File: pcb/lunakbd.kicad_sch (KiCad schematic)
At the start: 56 parts, among them SW1 Switch, SW10 Switch, SW11 Switch, SW12 Switch, SW13 Switch, SW14 Switch, SW15 Switch, SW16 Switch, SW17 Switch, SW18 Switch, SW19 Switch, SW2 Switch, SW20 Switch, SW21 Switch, SW22 Switch, SW23 Switch, SW24 Switch, SW25 Switch, SW26 Switch, SW27 Switch, SW28 Switch, SW3 Switch, SW4 Switch, SW5 Switch, SW6 Switch, SW7 Switch, SW8 Switch, SW9 Switch

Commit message: feat: pcb layout adjustments
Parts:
- SW28: footprint PCM_Switch_Keyboard_Cherry_MX:SW_Cherry_MX_PCB_1.00u -> PCM_Switch_Keyboard_Cherry_MX:SW_Cherry_MX_PCB_1.25u_90deg
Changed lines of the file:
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@@
 			)
 		)
-		(property "Footprint" "PCM_Switch_Keyboard_Cherry_MX:SW_Cherry_MX_PCB_1.00u"
+		(property "Footprint" "PCM_Switch_Keyboard_Cherry_MX:SW_Cherry_MX_PCB_1.25u_90deg"
 			(at 266.7 134.62 0)
 			(effects

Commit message: feat: complete schematic design
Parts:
- added D29: Diode, Diode_SMD:D_SOD-123, symbol Device:D_Small
- added J1: TRRS-PJ-320A, Connector_Audio:Jack_3.5mm_PJ320E_Horizontal, symbol Connector_Audio:AudioJack4
- added J2: Battery_Socket, Connector_JST:JST_PH_S2B-PH-K_1x02_P2.00mm_Horizontal, symbol Connector:Conn_01x02_Socket
- added J3: Conn_Display, kbd:OLED, symbol Connector_Generic:Conn_01x04
- added SW29: Reset_Button, Keebio-Parts:SW_Tactile_SPST_Angled_MJTP1117-no-mount, symbol Switch:SW_Push
- added SW30: Battery_Switch, PCM_marbastlib-various:SW_MSK12C02-HB, symbol Switch:SW_SPDT
- added SW31: RotaryEncoder_SW, Rotary_Encoder:RotaryEncoder_Alps_EC11E-Switch_Vertical_H20mm, symbol Device:RotaryEncoder_Switch
- added U1: ProMicro, PCM_marbastlib-xp-promicroish:SuperMini_nRF52840_H_USBup, symbol PCM_marbastlib-promicroish:Arduino_ProMicro
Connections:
- net col-0: now also U1.19 (F6)
- net col-1: now also SW31.S1, U1.20 (F7)
- net col-2: now also U1.21 (B1)
- net col-3: now also U1.22 (B3)
- net col-4: now also U1.23 (B2)
- net col-5: now also U1.24 (B6)
- net row-0: now also U1.7 (D4)
- net row-1: now also U1.8 (C6)
- net row-2: now also U1.9 (D7)
- net row-3: now also U1.10 (E6)
- net row-4: now also D29.1 (K), U1.11 (B4)
- new net: D29.2 (A), SW31.S2
- new net B+: J2.2 (Pin_2), U1.13 (B0)
- new net B-: J2.1 (Pin_1), SW30.1 (A)
- new net GND: J1.R1, J3.4 (Pin_4), SW29.2, SW30.2 (B), SW31.C, U1.14 (GND), U1.3 (GND), U1.4 (GND)
- new net VCC: J1.R2, J3.3 (Pin_3), U1.16 (VCC)
- new net data: J1.T, U1.2 (D2-RX)
- new net enc-a: SW31.A, U1.17 (F4)
- new net enc-b: SW31.B, U1.18 (F5)
- new net reset: SW29.1, U1.15 (RST)
- new net sda: J3.1 (Pin_1), U1.5 (D1)
- new net sdl: J3.2 (Pin_2), U1.6 (D0)
- no-connect marks 0 -> 3

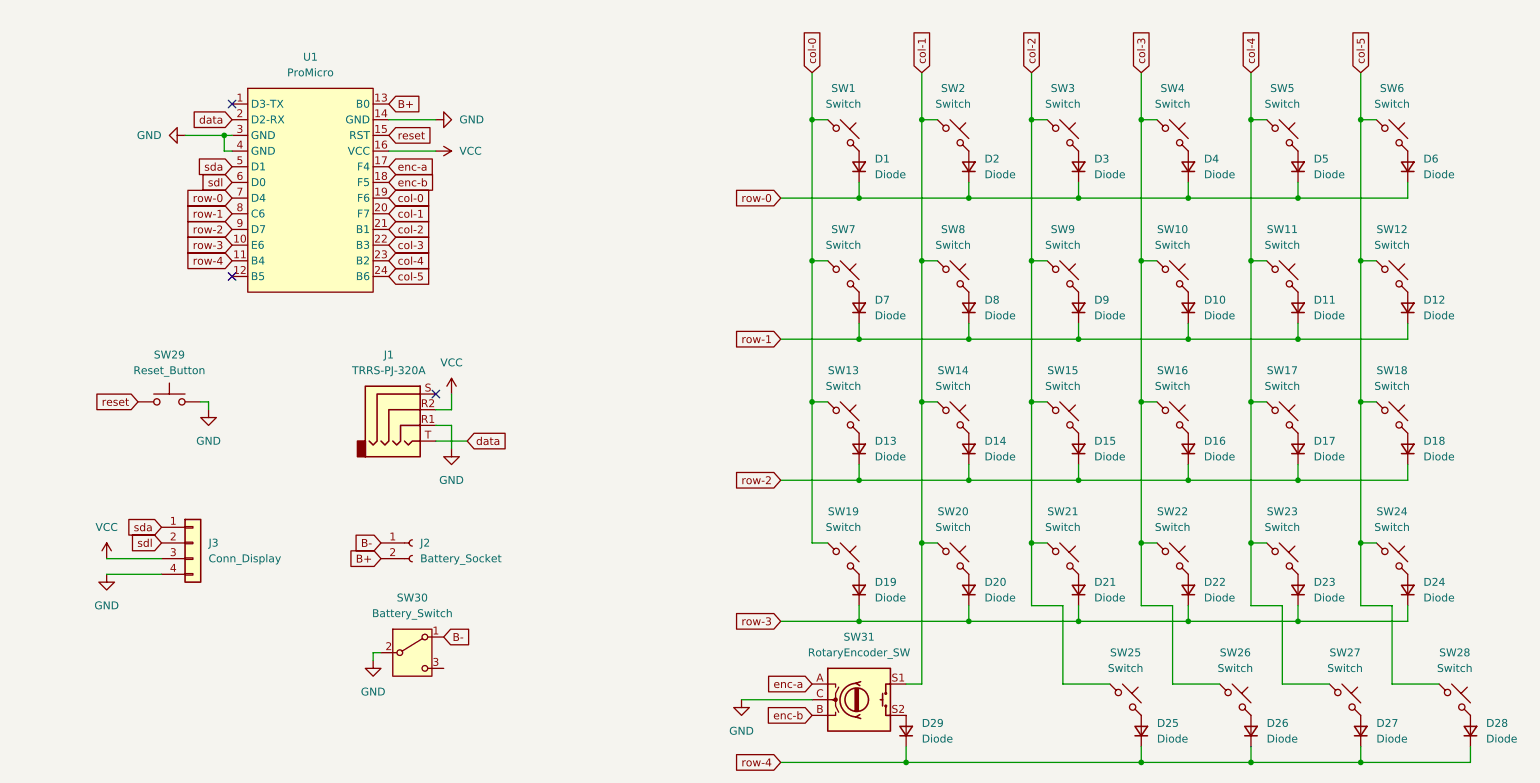
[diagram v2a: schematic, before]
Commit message: feat: update footprints and place promicro and oled display
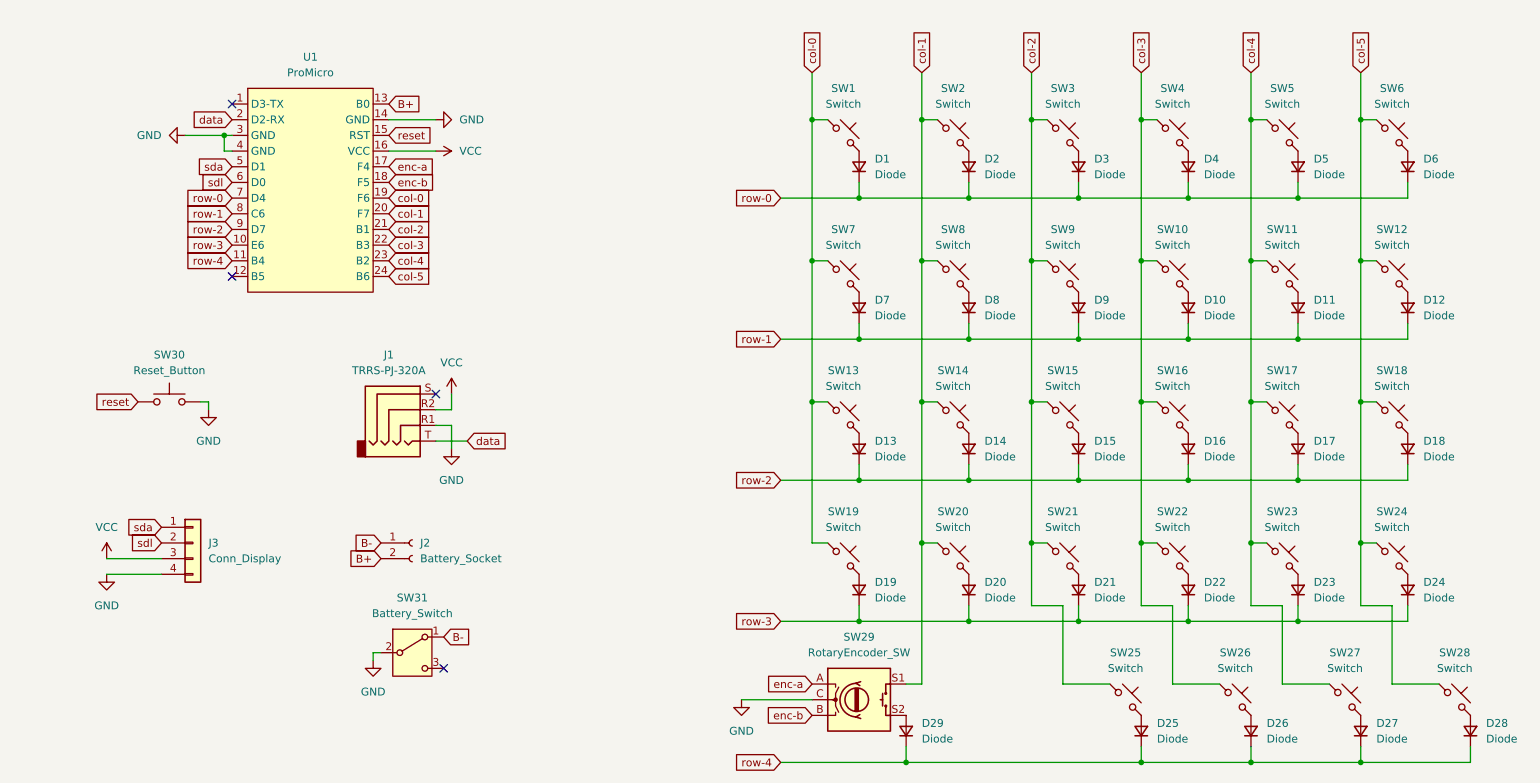
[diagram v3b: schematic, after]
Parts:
- J1: footprint Connector_Audio:Jack_3.5mm_PJ320E_Horizontal -> Keebio-Parts:TRRS-PJ-320A-no-Fmask
- SW1, SW10, SW11, SW12, SW13, SW14, SW15, SW16, SW17, SW18, SW19, SW2, SW20, SW21, SW22, SW23, SW24, SW25, SW26, SW27, SW3, SW4, SW5, SW6, SW7, SW8, SW9: footprint PCM_Switch_Keyboard_Cherry_MX:SW_Cherry_MX_PCB_1.00u -> PCM_Switch_Keyboard_Hotswap_Kailh:SW_Hotswap_Kailh_MX_1.00u
- SW28: footprint PCM_Switch_Keyboard_Cherry_MX:SW_Cherry_MX_PCB_1.25u_90deg -> PCM_Switch_Keyboard_Hotswap_Kailh:SW_Hotswap_Kailh_MX_1.25u_90deg
- SW30: renamed from SW29; footprint Keebio-Parts:SW_Tactile_SPST_Angled_MJTP1117-no-mount -> kbd:ResetSW
- SW31: renamed from SW30; footprint PCM_marbastlib-various:SW_MSK12C02-HB -> Button_Switch_SMD:SW_SPDT_PCM12
- renumbered SW31 to SW29
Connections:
- no-connect marks 3 -> 4

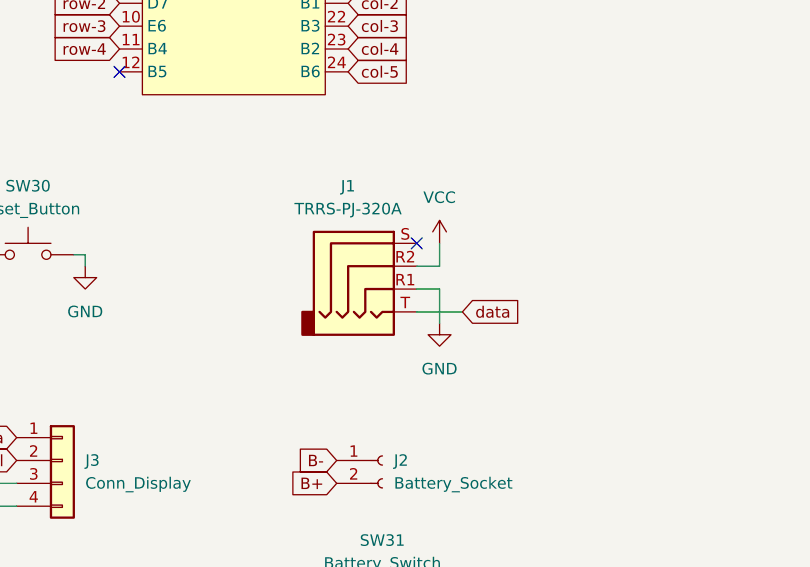
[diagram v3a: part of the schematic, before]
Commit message: feat: place trrs, battery socket and reset button
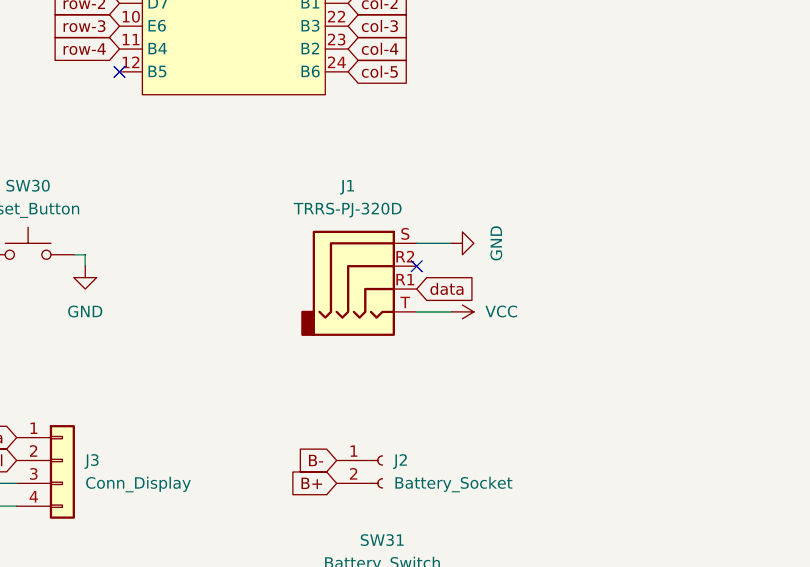
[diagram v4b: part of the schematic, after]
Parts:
- J1: value TRRS-PJ-320A -> TRRS-PJ-320D; footprint Keebio-Parts:TRRS-PJ-320A-no-Fmask -> Keebio-Parts:TRRS-PJ-320D
- SW30: footprint kbd:ResetSW -> kbd:SW_TL3330AF130QG
- SW31: footprint Button_Switch_SMD:SW_SPDT_PCM12 -> PCM_marbastlib-various:SW_MSK12C02-HB
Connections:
- net GND: now also J1.S; no longer J1.R1
- net VCC: now also J1.T; no longer J1.R2
- net data: now also J1.R1; no longer J1.T
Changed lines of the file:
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@@
 	)
 	(no_connect
-		(at 101.6 85.09)
-	)
-	(no_connect
 		(at 68.58 38.1)
 	)
@@
 		(at 102.87 129.54)
 	)
+	(no_connect
+		(at 101.6 87.63)
+	)
 	(wire
 		(pts
@@
 	(wire
 		(pts
-			(xy 182.88 109.22) (xy 180.34 109.22)
+			(xy 101.6 85.09) (xy 105.41 85.09)
 		)
 		(stroke
@@
 	(wire
 		(pts
-			(xy 223.52 99.06) (xy 241.3 99.06)
+			(xy 182.88 109.22) (xy 180.34 109.22)
 		)
 		(stroke
@@
 	(wire
 		(pts
-			(xy 170.18 76.2) (xy 187.96 76.2)
+			(xy 223.52 99.06) (xy 241.3 99.06)
 		)
 		(stroke
@@
 	(wire
 		(pts
-			(xy 182.88 63.5) (xy 180.34 63.5)
+			(xy 170.18 76.2) (xy 187.96 76.2)
 		)
 		(stroke
@@
 	(wire
 		(pts
-			(xy 170.18 73.66) (xy 170.18 76.2)
+			(xy 182.88 63.5) (xy 180.34 63.5)
 		)
 		(stroke
@@
 	(wire
 		(pts
-			(xy 203.2 119.38) (xy 198.12 119.38)
+			(xy 170.18 73.66) (xy 170.18 76.2)
 		)
 		(stroke
@@
 	(wire
 		(pts
-			(xy 251.46 33.02) (xy 251.46 40.64)
+			(xy 203.2 119.38) (xy 198.12 119.38)
 		)
 		(stroke
@@
 	(wire
 		(pts
-			(xy 187.96 73.66) (xy 187.96 76.2)
+			(xy 251.46 33.02) (xy 251.46 40.64)
 		)
 		(stroke
@@
 	(wire
 		(pts
-			(xy 106.68 92.71) (xy 101.6 92.71)
+			(xy 187.96 73.66) (xy 187.96 76.2)
 		)
 		(stroke
@@
 	(wire
 		(pts
-			(xy 104.14 87.63) (xy 101.6 87.63)
-		)
-		(stroke
-			(width 0)
-			(type default)
-		)
-	)
-	(wire
-		(pts
 			(xy 215.9 109.22) (xy 215.9 86.36)
 		)
@@
 	(wire
 		(pts
-			(xy 101.6 90.17) (xy 104.14 90.17)
-		)
-		(stroke
-			(width 0)
-			(type default)
-		)
-	)
-	(wire
-		(pts
 			(xy 241.3 76.2) (xy 259.08 76.2)
 		)
@@
 	(wire
 		(pts
-			(xy 104.14 90.17) (xy 104.14 93.98)
-		)
-		(stroke
-			(width 0)
-			(type default)
-		)
-	)
-	(wire
-		(pts
-			(xy 104.14 85.09) (xy 104.14 87.63)
-		)
-		(stroke
-			(width 0)
-			(type default)
-		)
-	)
-	(wire
-		(pts
 			(xy 198.12 109.22) (xy 198.12 86.36)
 		)
@@
 	(wire
 		(pts
+			(xy 101.6 92.71) (xy 105.41 92.71)
+		)
+		(stroke
+			(width 0)
+			(type default)
+		)
+	)
+	(wire
+		(pts
 			(xy 215.9 33.02) (xy 215.9 40.64)
 		)
@@
 		)
 	)
+	(global_label "data"
+		(shape input)
+		(at 101.6 90.17 0)
+		(fields_autoplaced yes)
+		(effects
+			(font
+				(size 1.27 1.27)
+			)
+			(justify left)
+		)
+		(property "Intersheetrefs" "${INTERSHEET_REFS}"
+			(at 108.7579 90.17 0)
+			(effects
+				(font
+					(size 1.27 1.27)
+				)
+				(justify left)
+				(hide yes)
+			)
+		)
+	)
 	(global_label "enc-b"
 		(shape input)
@@
 		)
 	)
-	(global_label "data"
-		(shape input)
-		(at 106.68 92.71 0)
-		(fields_autoplaced yes)
-		(effects
-			(font
-				(size 1.27 1.27)
-			)
-			(justify left)
-		)
-		(property "Intersheetrefs" "${INTERSHEET_REFS}"
-			(at 113.8379 92.71 0)
-			(effects
-				(font
-					(size 1.27 1.27)
-				)
-				(justify left)
-				(hide yes)
-			)
-		)
-	)
 	(global_label "sda"
 		(shape input)
@@
 	)
 	(symbol
-		(lib_id "power:GND")
-		(at 104.14 93.98 0)
-		(mirror y)
-		(unit 1)
-		(exclude_from_sim no)
-		(in_bom yes)
-		(on_board yes)
-		(dnp no)
-		(property "Reference" "#PWR02"
-			(at 104.14 100.33 0)
-			(effects
-				(font
-					(size 1.27 1.27)
-				)
-				(hide yes)
-			)
-		)
-		(property "Value" "GND"
-			(at 104.14 99.06 0)
-			(effects
-				(font
-					(size 1.27 1.27)
-				)
-			)
-		)
-		(property "Footprint" ""
-			(at 104.14 93.98 0)
-			(effects
-				(font
-					(size 1.27 1.27)
-				)
-				(hide yes)
-			)
-		)
-		(property "Datasheet" ""
-			(at 104.14 93.98 0)
-			(effects
-				(font
-					(size 1.27 1.27)
-				)
-				(hide yes)
-			)
-		)
-		(property "Description" "Power symbol creates a global label with name \"GND\" , ground"
-			(at 104.14 93.98 0)
-			(effects
-				(font
-					(size 1.27 1.27)
-				)
-				(hide yes)
-			)
-		)
-		(pin "1"
-		)
-		(instances
-			(project ""
-				(path "/c1259708-c799-472c-9386-b9d371ea7725"
-					(reference "#PWR02")
-					(unit 1)
-				)
-			)
-		)
-	)
-	(symbol
 		(lib_id "Device:D_Small")
 		(at 187.96 71.12 90)
@@
 	(symbol
 		(lib_id "power:VCC")
-		(at 104.14 85.09 0)
+		(at 105.41 92.71 270)
 		(unit 1)
 		(exclude_from_sim no)
@@
 		(fields_autoplaced yes)
 		(property "Reference" "#PWR01"
-			(at 104.14 88.9 0)
+			(at 101.6 92.71 0)
 			(effects
 				(font
@@
 		)
 		(property "Value" "VCC"
-			(at 104.14 80.01 0)
+			(at 109.22 92.71 90)
 			(effects
 				(font
 					(size 1.27 1.27)
 				)
+				(justify left)
 			)
 		)
 		(property "Footprint" ""
-			(at 104.14 85.09 0)
+			(at 105.41 92.71 0)
 			(effects
 				(font
@@
 		)
 		(property "Datasheet" ""
-			(at 104.14 85.09 0)
+			(at 105.41 92.71 0)
 			(effects
 				(font
@@
 		)
 		(property "Description" "Power symbol creates a global label with name \"VCC\""
-			(at 104.14 85.09 0)
+			(at 105.41 92.71 0)
 			(effects
 				(font
@@
 		)
 		(instances
-			(project ""
+			(project "lunakbd"
 				(path "/c1259708-c799-472c-9386-b9d371ea7725"
 					(reference "#PWR01")
@@
 			)
 		)
-		(property "Footprint" "kbd:ResetSW"
+		(property "Footprint" "kbd:SW_TL3330AF130QG"
 			(at 58.42 81.28 0)
 			(effects
@@
 	)
 	(symbol
+		(lib_id "power:GND")
+		(at 105.41 85.09 90)
+		(mirror x)
+		(unit 1)
+		(exclude_from_sim no)
+		(in_bom yes)
+		(on_board yes)
+		(dnp no)
+		(property "Reference" "#PWR011"
+			(at 111.76 85.09 0)
+			(effects
+				(font
+					(size 1.27 1.27)
+				)
+				(hide yes)
+			)
+		)
+		(property "Value" "GND"
+			(at 110.49 85.09 0)
+			(effects
+				(font
+					(size 1.27 1.27)
+				)
+			)
+		)
+		(property "Footprint" ""
+			(at 105.41 85.09 0)
+			(effects
+				(font
+					(size 1.27 1.27)
+				)
+				(hide yes)
+			)
+		)
+		(property "Datasheet" ""
+			(at 105.41 85.09 0)
+			(effects
+				(font
+					(size 1.27 1.27)
+				)
+				(hide yes)
+			)
+		)
+		(property "Description" "Power symbol creates a global label with name \"GND\" , ground"
+			(at 105.41 85.09 0)
+			(effects
+				(font
+					(size 1.27 1.27)
+				)
+				(hide yes)
+			)
+		)
+		(pin "1"
+		)
+		(instances
+			(project "lunakbd"
+				(path "/c1259708-c799-472c-9386-b9d371ea7725"
+					(reference "#PWR011")
+					(unit 1)
+				)
+			)
+		)
+	)
+	(symbol
 		(lib_id "Switch:SW_Push_45deg")
 		(at 203.2 66.04 0)
@@
 			)
 		)
-		(property "Value" "TRRS-PJ-320A"
+		(property "Value" "TRRS-PJ-320D"
 			(at 93.98 81.28 0)
 			(effects
@@
 			)
 		)
-		(property "Footprint" "Keebio-Parts:TRRS-PJ-320A-no-Fmask"
+		(property "Footprint" "Keebio-Parts:TRRS-PJ-320D"
 			(at 96.52 87.63 0)
 			(effects
@@
 			)
 		)
-		(property "Footprint" "Button_Switch_SMD:SW_SPDT_PCM12"
+		(property "Footprint" "PCM_marbastlib-various:SW_MSK12C02-HB"
 			(at 97.79 127 0)
 			(effects

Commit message: feat: make all footprints inversibles
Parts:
- D1, D10, D11, D12, D13, D14, D15, D16, D17, D18, D19, D2, D20, D21, D22, D23, D24, D25, D26, D27, D28, D29, D3, D4, D5, D6, D7, D8, D9: footprint Diode_SMD:D_SOD-123 -> Library:D_SOD-123
- J1: footprint Keebio-Parts:TRRS-PJ-320D -> Library:TRRS-PJ-320D
- SW1, SW10, SW11, SW12, SW13, SW14, SW15, SW16, SW17, SW18, SW19, SW2, SW20, SW21, SW22, SW23, SW24, SW25, SW26, SW27, SW3, SW4, SW5, SW6, SW7, SW8, SW9: footprint PCM_Switch_Keyboard_Hotswap_Kailh:SW_Hotswap_Kailh_MX_1.00u -> Library:SW_Hotswap_Kailh_MX_1.00u
- SW28: footprint PCM_Switch_Keyboard_Hotswap_Kailh:SW_Hotswap_Kailh_MX_1.25u_90deg -> Library:SW_Hotswap_Kailh_MX_1.25u_90deg
- SW30: footprint kbd:SW_TL3330AF130QG -> Library:SW_TL3330AF130QG
- SW31: footprint PCM_marbastlib-various:SW_MSK12C02-HB -> Library:SW_MSK12C02-HB

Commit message: feat: trace routes
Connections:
- net GND: now also SW30.1; no longer SW30.2
- net reset: now also SW30.2; no longer SW30.1
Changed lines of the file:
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@@
 		(lib_id "Switch:SW_Push")
 		(at 58.42 86.36 0)
+		(mirror y)
 		(unit 1)
 		(exclude_from_sim no)
@@
 		(on_board yes)
 		(dnp no)
-		(fields_autoplaced yes)
 		(property "Reference" "SW30"
 			(at 58.42 78.74 0)

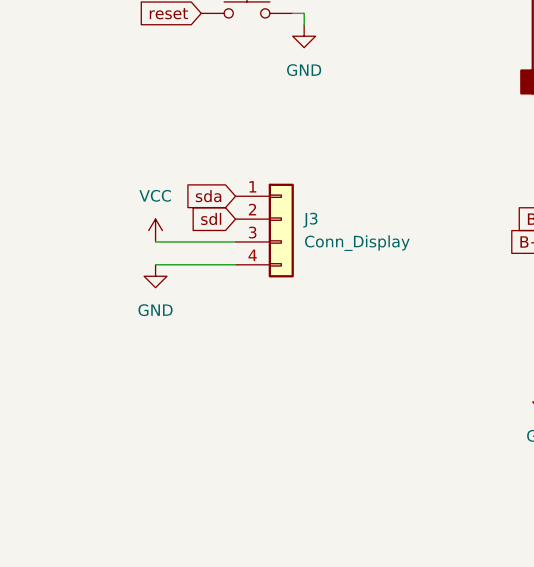
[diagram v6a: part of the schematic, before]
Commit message: fix: connection for oled inversion
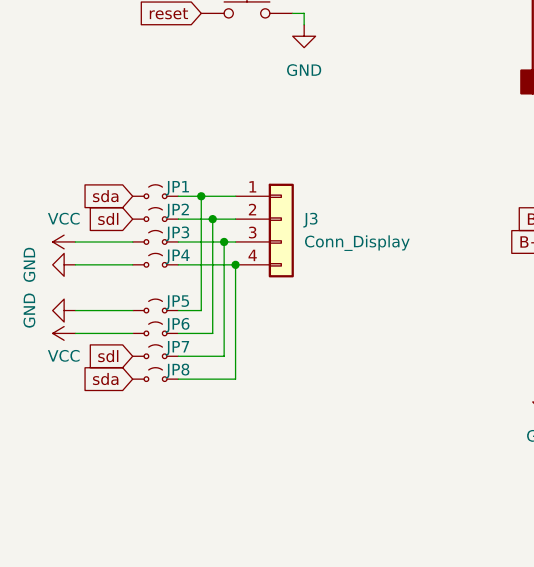
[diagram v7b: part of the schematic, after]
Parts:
- added JP1, JP2, JP3, JP4, JP5, JP6, JP7, JP8: Jumper, Jumper:SolderJumper-2_P1.3mm_Open_RoundedPad1.0x1.5mm, symbol Jumper:Jumper_2_Small_Open
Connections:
- net GND: now also JP4.1 (A), JP5.1 (A); no longer J3.4 (Pin_4)
- net VCC: now also JP3.1 (A), JP6.1 (A); no longer J3.3 (Pin_3)
- net sda: now also JP1.1 (A), JP8.1 (A); no longer J3.1 (Pin_1)
- net sdl: now also JP2.1 (A), JP7.1 (A); no longer J3.2 (Pin_2)
- new net: J3.2 (Pin_2), JP2.2 (B), JP6.2 (B)
- new net: J3.1 (Pin_1), JP1.2 (B), JP5.2 (B)
- new net: J3.4 (Pin_4), JP4.2 (B), JP8.2 (B)
- new net: J3.3 (Pin_3), JP3.2 (B), JP7.2 (B)
